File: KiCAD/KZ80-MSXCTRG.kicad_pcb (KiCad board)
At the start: 2 copper layers, 100 x 75 mm, 23 parts, among them J1 MSX SLOT-A, J2 SBC8080 BUS, J3 SLT-JP, J4 Z80 CTRL, J5 PPI PORT-A, U1 74HC139, U2 74HC153, U3 74HC32, U4 74HC00, U5 74HC00

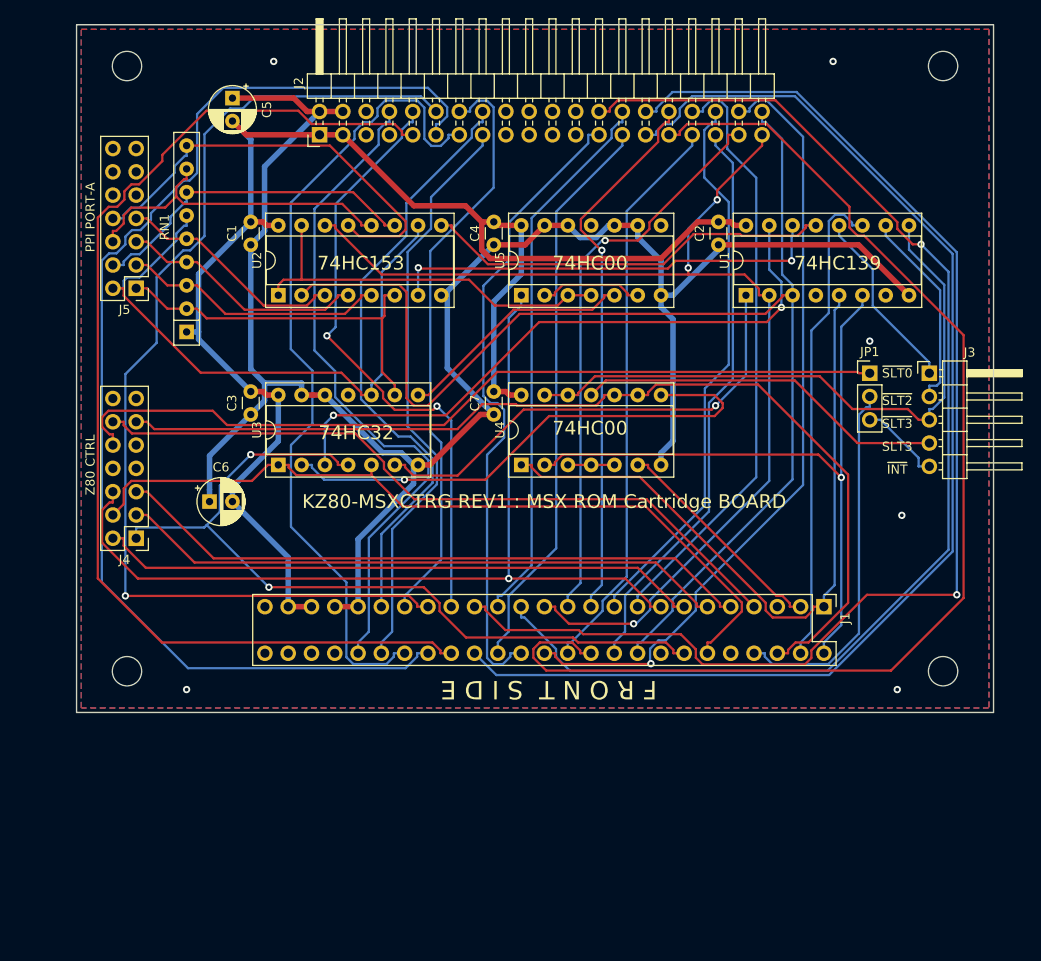
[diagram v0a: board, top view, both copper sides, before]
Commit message: プリントパターン見直し
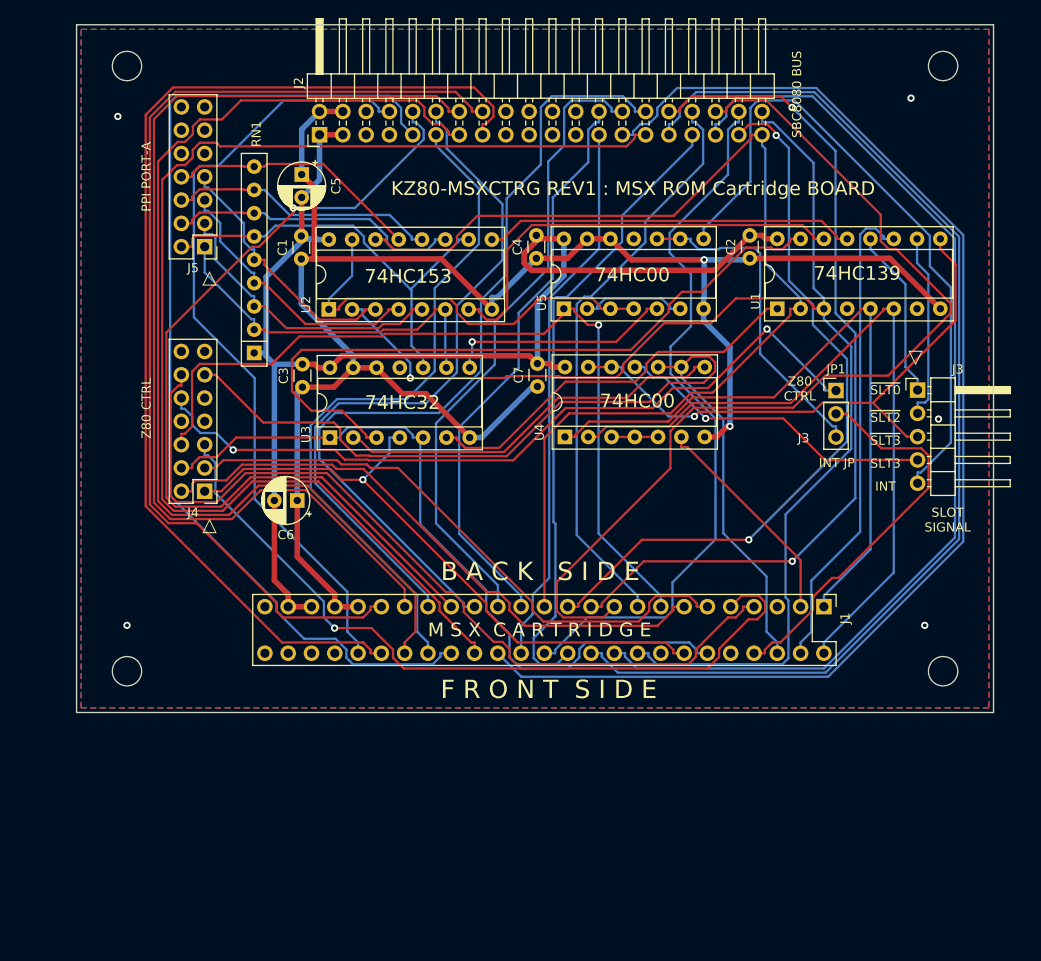
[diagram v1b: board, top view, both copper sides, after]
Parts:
- moved C5 11.2 mm to (141.6, 94.3)
- moved C6 9.57 mm to (141.1, 129.9), turned to 180 degrees
- moved J4 9.06 mm to (131.0, 128.9)
- moved J5 8.74 mm to (131.0, 102.2)
- moved RN1 7.72 mm to (136.4, 113.8)
- moved C3 6.37 mm to (141.6, 117.5)
- moved U3 6.37 mm to (144.6, 123.0)
- moved C1 5.72 mm to (141.5, 103.5)
- moved U2 5.72 mm to (144.5, 109.0)
- moved C7 5.65 mm to (167.3, 117.5)
- moved U4 5.65 mm to (170.3, 123.0)
- moved C4 4.87 mm to (167.1, 103.5)
- moved U5 4.87 mm to (170.1, 109.0)
- moved JP1 4.14 mm to (199.8, 117.9)
- moved C2 3.72 mm to (190.4, 103.5)
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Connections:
- J3 pad 5: /~INT-J -> /INT-J
- JP1 pad 3: /~INT-J -> Net-(JP1-Pad3)
- U5 pad 10: GND -> Net-(JP1-Pad3)
- U5 pad 8: Net-(U5-Pad8) -> /INT-J
- U5 pad 9: GND -> Net-(JP1-Pad3)
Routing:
- net /A2: track 62.2 -> 138.0 mm
- net /INT-J: track 0.00 -> 72.1 mm
- net /A1: track 133.5 -> 63.3 mm, vias 1 -> 0
- net /D6: track 63.8 -> 119.0 mm
- net /D2: track 130.2 -> 75.8 mm
- net /A10: track 62.7 -> 112.1 mm
- net /D5: track 64.2 -> 112.9 mm
- net /A5: track 139.2 -> 91.7 mm, vias 1 -> 0
- net /D7: track 66.0 -> 112.3 mm
- net /A11: track 61.0 -> 106.0 mm
- net /D3: track 115.7 -> 76.3 mm, vias 1 -> 0
- net Net-(JP1-Pad3): track 0.00 -> 35.9 mm
- net /A7: track 59.7 -> 94.3 mm, vias 1 -> 2
- net /D1: track 67.0 -> 97.5 mm, vias 2 -> 1
- net /D4: track 90.1 -> 117.3 mm
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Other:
- board text added: "B A C K S I D E"
- board text added: "INT"
- board text added: "INT JP"
- board text added: "J3"
- board text added: "M S X C A R T R I D G E"
- board text added: "SBC8080 BUS"
- board text added: "SLOT SIGNAL"
- board text added: "△"
- board text removed: "~INT"

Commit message: REV1基板(1WAIT回路追加) ガーバーデータ出力
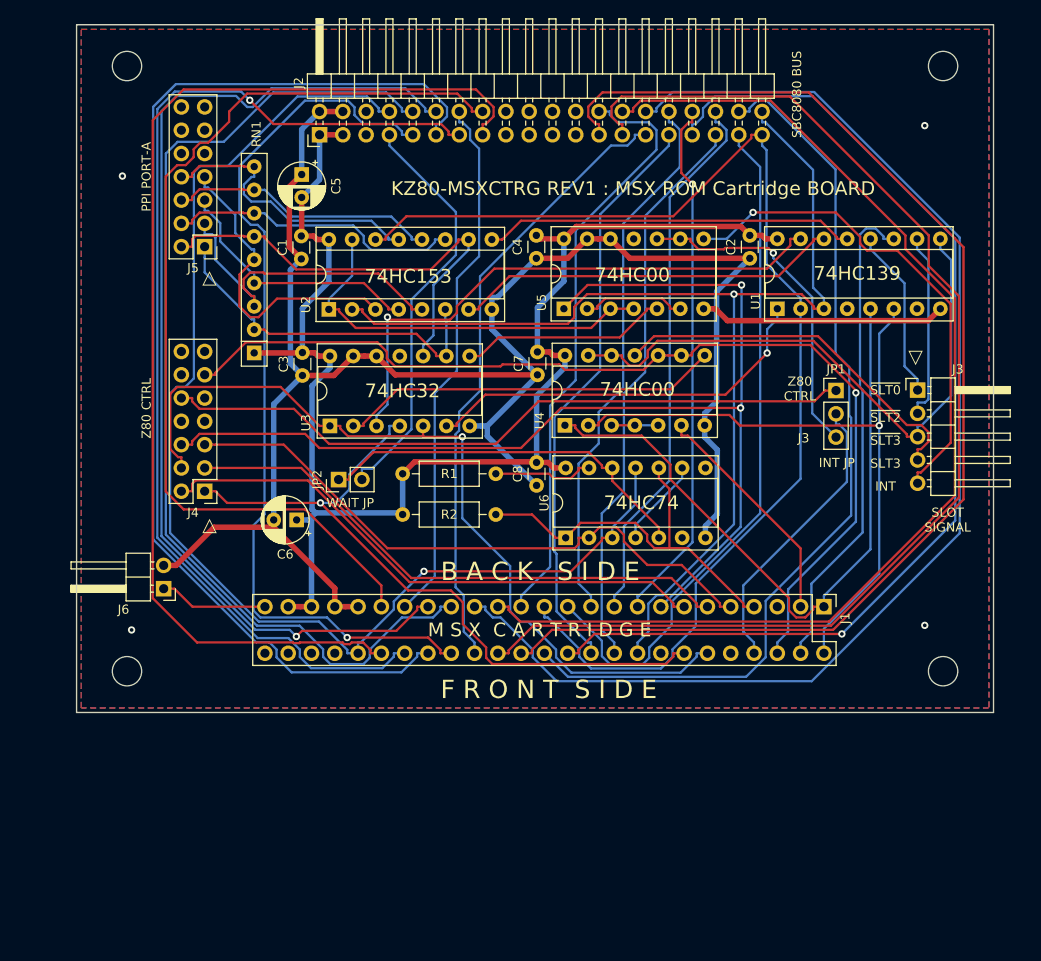
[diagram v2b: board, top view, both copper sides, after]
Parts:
- added C8: 0.1u, Capacitor_THT:C_Disc_D3.0mm_W1.6mm_P2.50mm, F.Cu at (167.2, 128.2)
- added J6: SOUND, Connector_PinHeader_2.54mm:PinHeader_1x02_P2.54mm_Horizontal, F.Cu at (126.5, 139.5)
- added JP2: WAIT JP, Connector_PinHeader_2.54mm:PinHeader_1x02_P2.54mm_Vertical, F.Cu at (145.6, 127.6)
- added R1: 10k, Resistor_THT:R_Axial_DIN0207_L6.3mm_D2.5mm_P10.16mm_Horizontal, F.Cu at (152.6, 127.0)
- added R2: 10k, Resistor_THT:R_Axial_DIN0207_L6.3mm_D2.5mm_P10.16mm_Horizontal, F.Cu at (152.6, 131.4)
- added U6: 74HC74, Package_DIP:DIP-14_W7.62mm_Socket, F.Cu at (170.3, 133.9)
- moved C6 2.12 mm to (141.0, 132.0)
- moved C3 1.27 mm to (141.6, 116.2)
- moved C7 1.27 mm to (167.3, 116.2)
- moved U3 1.27 mm to (144.6, 121.8)
- moved U4 1.27 mm to (170.3, 121.7)
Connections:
- C6 pad 1: GND -> VCC
- C6 pad 2: VCC -> GND
- J1 pad 7: /~WAIT -> /~WAIT_C
- J2 pad 7: Net-(J2-Pad7) -> /RDYIN
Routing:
- net /~WAIT: track 92.1 -> 0.00 mm
- net /A0: track 60.1 -> 135.3 mm
- net /A4: track 135.5 -> 67.7 mm
- net /A6: track 121.5 -> 63.6 mm
- net /D5: track 112.9 -> 58.5 mm
- net /A3: track 70.4 -> 124.7 mm
- net /CLK: track 85.1 -> 135.7 mm, vias 0 -> 1
- net /A10: track 112.1 -> 62.2 mm
- net /A8: track 69.5 -> 117.3 mm, vias 0 -> 1
- net /D2: track 75.8 -> 122.6 mm
- net /A11: track 106.0 -> 59.8 mm
- net /A5: track 91.7 -> 137.8 mm
- net /RDYIN: track 0.00 -> 45.5 mm
- net /~WAIT_C: track 0.00 -> 43.5 mm
- net Net-(JP2-Pad1): track 0.00 -> 41.9 mm
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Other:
- board text added: "74HC74"
- board text added: "WAIT JP"

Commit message: パターン改良ぬ
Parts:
- added C10: 10u, Capacitor_THT:CP_Radial_D5.0mm_P2.50mm, F.Cu at (138.6, 155.1)
- added C11: 10u, Capacitor_THT:CP_Radial_D5.0mm_P2.50mm, F.Cu at (120.8, 160.2)
- added C9: 10u, Capacitor_THT:CP_Radial_D5.0mm_P2.50mm, F.Cu at (120.8, 138.6)
- added J7: MSX SLOT-B, PCBEdge:PCB_Edge_Conn_2x25_P2.54mm_Vertical, F.Cu at (198.3, 166.6)
- added R3: 10k, Resistor_THT:R_Axial_DIN0207_L6.3mm_D2.5mm_P10.16mm_Horizontal, F.Cu at (164.0, 123.4)
- added R4: 10k, Resistor_THT:R_Axial_DIN0207_L6.3mm_D2.5mm_P10.16mm_Horizontal, F.Cu at (167.8, 123.4)
- added R5: 10k, Resistor_THT:R_Axial_DIN0207_L6.3mm_D2.5mm_P10.16mm_Horizontal, F.Cu at (195.7, 133.6)
- added R6: 22k, Resistor_THT:R_Axial_DIN0207_L6.3mm_D2.5mm_P10.16mm_Horizontal, F.Cu at (129.7, 148.8)
- added R7: 22k, Resistor_THT:R_Axial_DIN0207_L6.3mm_D2.5mm_P10.16mm_Horizontal, F.Cu at (128.4, 160.2)
- moved J6 32.6 mm to (120.8, 171.7)
- moved C7 3.81 mm to (171.1, 116.2)
- moved C8 3.81 mm to (171.0, 128.2)
- moved U4 3.81 mm to (174.1, 121.7)
- moved U6 3.81 mm to (174.2, 133.9)
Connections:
- J1 pad 49: Net-(J1-Pad49) -> Net-(C9-Pad1)
- J6 pad 1: Net-(J1-Pad49) -> Net-(J6-Pad1)
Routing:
- net /A4: track 67.7 -> 197.6 mm
- net /A1: track 65.4 -> 190.8 mm
- net GND: track 229.7 -> 347.9 mm
- net /A7: track 59.8 -> 169.3 mm, vias 0 -> 1
- net /A6: track 63.6 -> 171.6 mm, vias 0 -> 2
- net /CLK: track 135.7 -> 234.0 mm, vias 1 -> 2
- net /A11: track 59.8 -> 151.4 mm, vias 0 -> 1
- net VCC: track 161.9 -> 246.8 mm, vias 0 -> 8
- net /D5: track 58.5 -> 140.2 mm, vias 0 -> 1
- net /D0: track 98.4 -> 172.0 mm, vias 1 -> 0
- net /A2: track 132.6 -> 197.3 mm
- net /A10: track 62.2 -> 123.1 mm, vias 0 -> 2
- net /D1: track 113.1 -> 170.2 mm
- net /~M1: track 67.6 -> 123.9 mm, vias 0 -> 3
- net /~SLT2: track 20.5 -> 76.3 mm, vias 0 -> 1
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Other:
- board size 100 x 75 mm -> 100 x 100 mm
- board text added: "KZ80-MSXCTRG REV2 : MSX ROM Cartridge BOARD"
- board text added: "M S X C A R T R I D G E - 1"
- board text added: "M S X C A R T R I D G E - 2"
- board text removed: "KZ80-MSXCTRG REV1 : MSX ROM Cartridge BOARD"
- board text removed: "M S X C A R T R I D G E"

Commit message: ガーバーデータ出力
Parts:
- moved J1 25.0 mm to (198.5, 169.0)
- moved J7 22.6 mm to (198.5, 144.0)
- moved C9 22.3 mm to (134.5, 156.2)
- moved C11 6.94 mm to (126.5, 156.2)
- moved C10 4.55 mm to (143.0, 156.2)
- moved C6 4.00 mm to (137.0, 132.0), turned to 0 degrees
- moved R7 2.98 mm to (129.5, 163.0)
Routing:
- net /D1: track 170.2 -> 82.9 mm
- net /D0: track 172.0 -> 85.2 mm
- net /A7: track 169.3 -> 83.7 mm, vias 1 -> 0
- net /A6: track 171.6 -> 86.0 mm, vias 2 -> 0
- net /A3: track 94.9 -> 169.8 mm, vias 3 -> 0
- net /CLK: track 234.0 -> 300.3 mm, vias 2 -> 0
- net /A11: track 151.4 -> 85.9 mm
- net GND: track 347.9 -> 304.2 mm
- net /A13: track 121.5 -> 162.7 mm, vias 1 -> 0
- net /~M1: track 123.9 -> 92.0 mm, vias 3 -> 0
- net /D4: track 165.0 -> 134.2 mm, vias 0 -> 1
- net /~SLT1: track 52.9 -> 81.2 mm
- net /~WAIT_C: track 97.0 -> 70.3 mm, vias 2 -> 0
- net /~CS2: track 118.8 -> 92.2 mm, vias 2 -> 1
- net /D2: track 128.0 -> 154.0 mm
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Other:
- board text added: "1"
- board text added: "2"
